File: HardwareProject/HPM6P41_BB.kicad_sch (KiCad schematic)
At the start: 6 parts

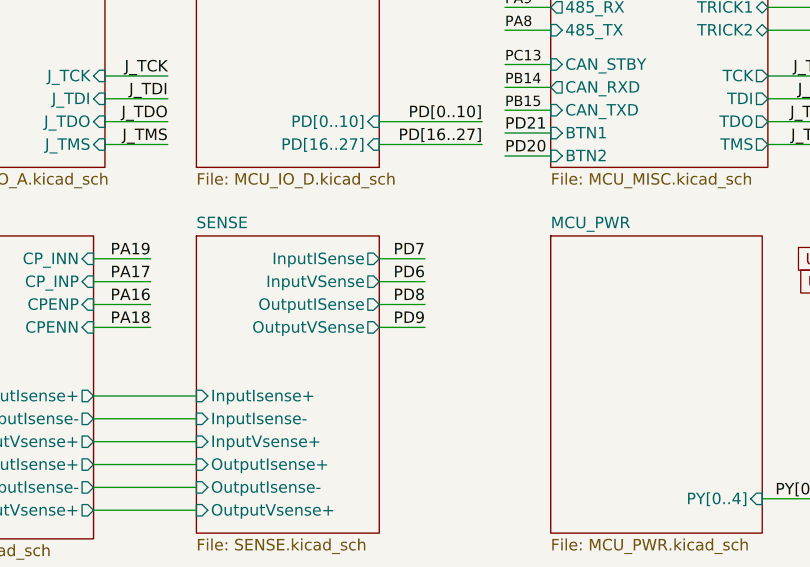
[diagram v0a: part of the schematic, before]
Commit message: 修改了UCC27211A封装，此芯片此前的封装均错误 修改了采样线布局，为SAR ADC加入前置RC
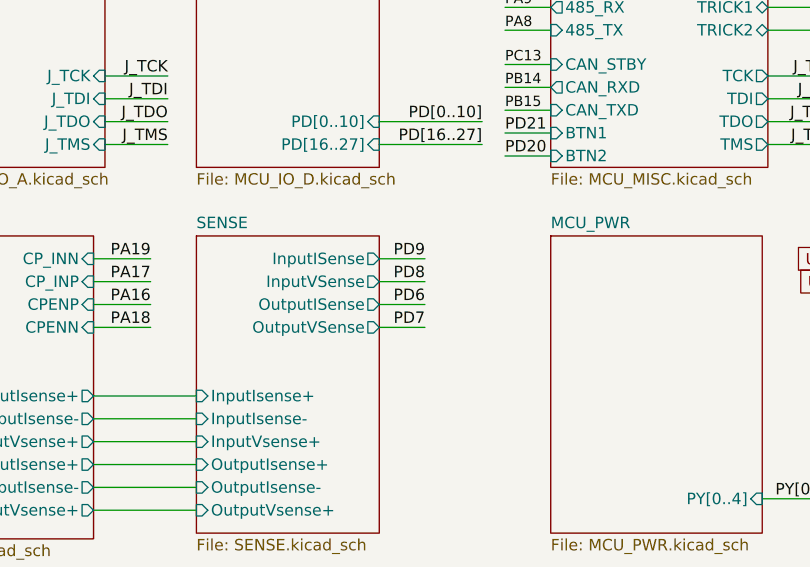
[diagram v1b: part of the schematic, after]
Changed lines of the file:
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@@
 	)
 	(label "PD8"
-		(at 187.96 101.6 180)
+		(at 187.96 99.06 180)
 		(effects
 			(font
@@
 	)
 	(label "PD6"
-		(at 187.96 99.06 180)
+		(at 187.96 101.6 180)
 		(effects
 			(font
@@
 	)
 	(label "PD7"
-		(at 187.96 96.52 180)
+		(at 187.96 104.14 180)
 		(effects
 			(font
@@
 	)
 	(label "PD9"
-		(at 187.96 104.14 180)
-		(effects
-			(font
+		(at 187.96 96.52 180)
+		(effects
+			(font

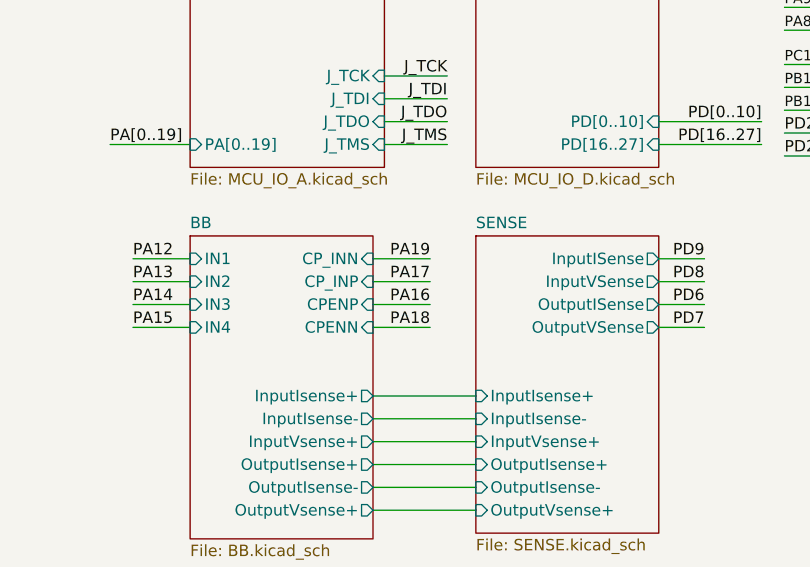
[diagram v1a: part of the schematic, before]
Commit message: 换掉UCC27519，它居然要55%VDD才到逻辑高，换成UCC2751
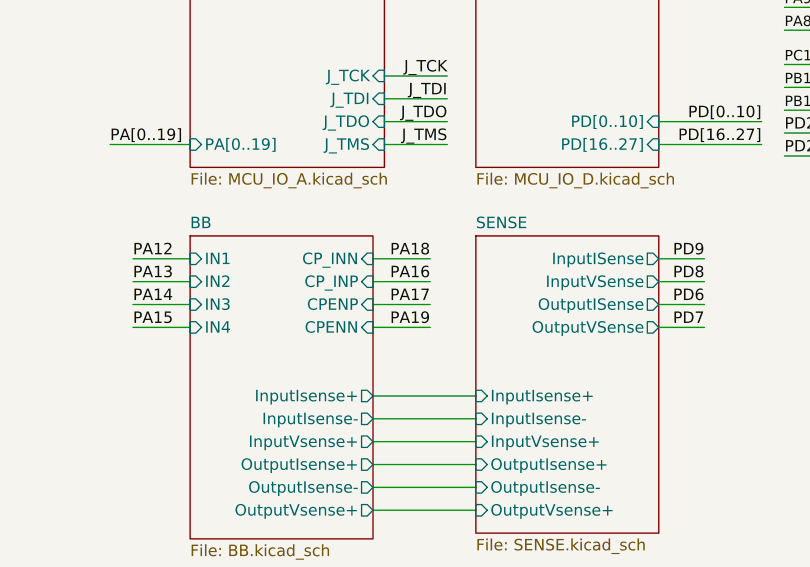
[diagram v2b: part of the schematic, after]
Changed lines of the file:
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@@
 	)
 	(label "PA16"
-		(at 157.48 101.6 180)
+		(at 157.48 99.06 180)
 		(effects
 			(font
@@
 	)
 	(label "PA17"
-		(at 157.48 99.06 180)
+		(at 157.48 101.6 180)
 		(effects
 			(font
@@
 	)
 	(label "PA19"
-		(at 157.48 96.52 180)
+		(at 157.48 104.14 180)
 		(effects
 			(font
@@
 	)
 	(label "PA18"
-		(at 157.48 104.14 180)
-		(effects
-			(font
+		(at 157.48 96.52 180)
+		(effects
+			(font

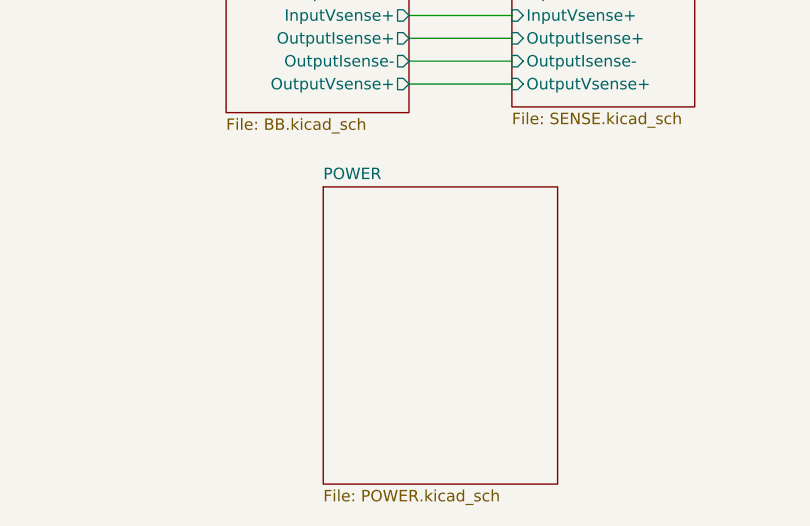
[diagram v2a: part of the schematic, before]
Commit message: 外置核心电压SYR838以改善ADC噪声
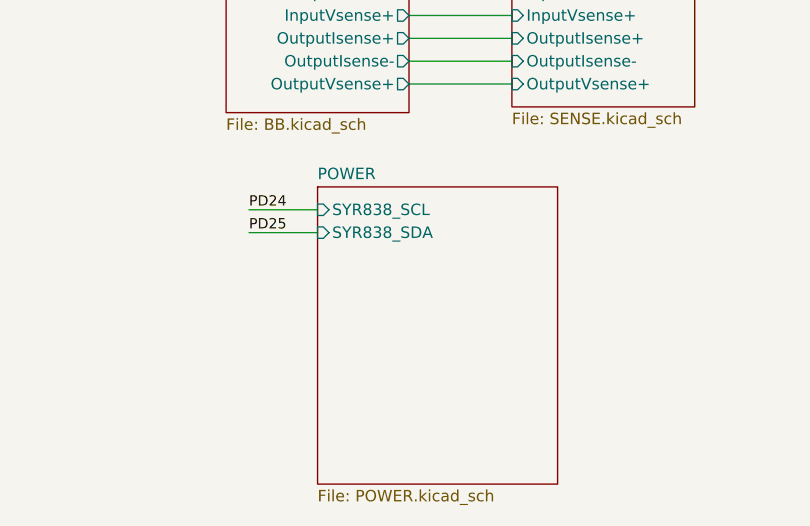
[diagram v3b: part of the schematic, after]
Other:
- sheet POWER ports: added SYR838_SCL, SYR838_SDA; removed none
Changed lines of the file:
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@@
 	(wire
 		(pts
+			(xy 133.35 138.43) (xy 140.97 138.43)
+		)
+		(stroke
+			(width 0)
+			(type default)
+		)
+	)
+	(wire
+		(pts
 			(xy 196.85 85.09) (xy 201.93 85.09)
 		)
@@
 	(wire
 		(pts
+			(xy 140.97 140.97) (xy 133.35 140.97)
+		)
+		(stroke
+			(width 0)
+			(type default)
+		)
+	)
+	(wire
+		(pts
 			(xy 182.88 104.14) (xy 187.96 104.14)
 		)
@@
 		)
 	)
+	(label "PD25"
+		(at 133.35 140.97 0)
+		(effects
+			(font
+				(size 1.15 1.15)
+				(color 36 73 139 1)
+			)
+			(justify left bottom)
+		)
+	)
 	(label "PA3"
 		(at 196.85 58.42 0)
@@
 		)
 	)
+	(label "PD24"
+		(at 133.35 138.43 0)
+		(effects
+			(font
+				(size 1.15 1.15)
+				(color 36 73 139 1)
+			)
+			(justify left bottom)
+		)
+	)
 	(label "PD20"
 		(at 196.85 85.09 0)
@@
 	)
 	(sheet
-		(at 141.605 135.89)
-		(size 26.035 33.02)
+		(at 140.97 135.89)
+		(size 26.67 33.02)
 		(exclude_from_sim no)
 		(in_bom yes)
@@
 		)
 		(property "Sheetname" "POWER"
-			(at 141.605 135.1784 0)
+			(at 140.97 135.1784 0)
 			(effects
 				(font
@@
 		)
 		(property "Sheetfile" "POWER.kicad_sch"
-			(at 141.605 169.4946 0)
+			(at 140.97 169.4946 0)
 			(effects
 				(font
@@
 			)
 		)
+		(pin "SYR838_SCL" input
+			(at 140.97 138.43 180)
+			(effects
+				(font
+					(size 1.27 1.27)
+				)
+				(justify left)
+			)
+		)
+		(pin "SYR838_SDA" input
+			(at 140.97 140.97 180)
+			(effects
+				(font
+					(size 1.27 1.27)
+				)
+				(justify left)
+			)
+		)

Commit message: 换其他电感之前暂存一下
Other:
- sheet BB ports: added ISENSE+, ISENSE-; removed InputIsense+, InputIsense-, OutputIsense+, OutputIsense-
- sheet MCU_MISC ports: added none; removed TCK, TDI, TDO, TMS
- sheet MCU_MISC2 ports: added ISO_RX, ISO_TX, TCK, TDI, TDO, TMS; removed none
- sheet SENSE ports: added ISENSE+, ISENSE-; removed InputIsense+, InputIsense-, OutputIsense+, OutputIsense-

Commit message: 完成Rev4 电源 驱动 模拟 IO
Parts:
- added R56: 0Ω, Resistor_SMD:R_0603_1608Metric, symbol Device:R
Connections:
- net DCDC_GND: now also R56.2
- new net GNDA: R56.1
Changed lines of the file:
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@@
 	)
 	(junction
-		(at 187.96 31.75)
+		(at 188.0119 31.75)
 		(diameter 0)
 		(color 0 0 0 0)
@@
 	(wire
 		(pts
+			(xy 188.0119 31.75) (xy 195.58 31.75)
+		)
+		(stroke
+			(width 0)
+			(type default)
+		)
+	)
+	(wire
+		(pts
 			(xy 182.88 99.06) (xy 187.96 99.06)
 		)
@@
 	(wire
 		(pts
-			(xy 187.96 31.75) (xy 195.58 31.75)
+			(xy 187.96 31.75) (xy 188.0119 31.75)
 		)
 		(stroke
@@
 	(wire
 		(pts
-			(xy 180.34 31.75) (xy 187.96 31.75)
+			(xy 180.34 31.75) (xy 180.3919 31.75)
 		)
 		(stroke
@@
 					(unit 1)
 				)
+			)
+		)
+	)
+	(symbol
+		(lib_id "Device:R")
+		(at 184.2019 31.75 90)
+		(mirror x)
+		(unit 1)
+		(exclude_from_sim no)
+		(in_bom yes)
+		(on_board yes)
+		(dnp no)
+		(property "Reference" "R56"
+			(at 184.2019 29.464 90)
+			(effects
+				(font
+					(size 1.27 1.27)
+				)
+			)
+		)
+		(property "Value" "0Ω"
+			(at 184.2019 31.75 90)
+			(effects
+				(font
+					(size 1.27 1.27)
+				)
+			)
+		)
+		(property "Footprint" "Resistor_SMD:R_0603_1608Metric"
+			(at 184.2019 29.972 90)
+			(effects
+				(font
+					(size 1.27 1.27)
+				)
+				(hide yes)
+			)
+		)
+		(property "Datasheet" "~"
+			(at 184.2019 31.75 0)
+			(effects
+				(font
+					(size 1.27 1.27)
+				)
+				(hide yes)
+			)
+		)
+		(property "Description" ""
+			(at 184.2019 31.75 0)
+			(effects
+				(font
+					(size 1.27 1.27)
+				)
+				(hide yes)
+			)
+		)
+		(pin "1"
+		)
+		(pin "2"
+		)
+		(instances
+			(project "HPM6P41_BB"
+				(path "/714b8a30-f9a7-49d4-a000-bc20c4884c7a"
+					(reference "R56")
+					(unit 1)
+				)

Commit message: rev4修改核心供电前保存（当前SYR838）
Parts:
- renumbered H4 to H1, H3 to H2, H2 to H3, H1 to H4, R56 to R1
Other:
- sheet BB ports: added ISENSE2+, ISENSE2-; removed none
- sheet SENSE ports: added AvgSns, IAvg+, IAvg-, PeakSns; removed InputISense, OutputISense
